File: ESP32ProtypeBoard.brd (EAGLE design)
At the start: 78.7 x 54.6 mm, 90 parts, among them IC1 ACT4088US-T, IC2 SI4431BDY, J4 VCC_TERMINAL, Q4 BSS138, U1 3.3V, U2 ESP-WROOM-32

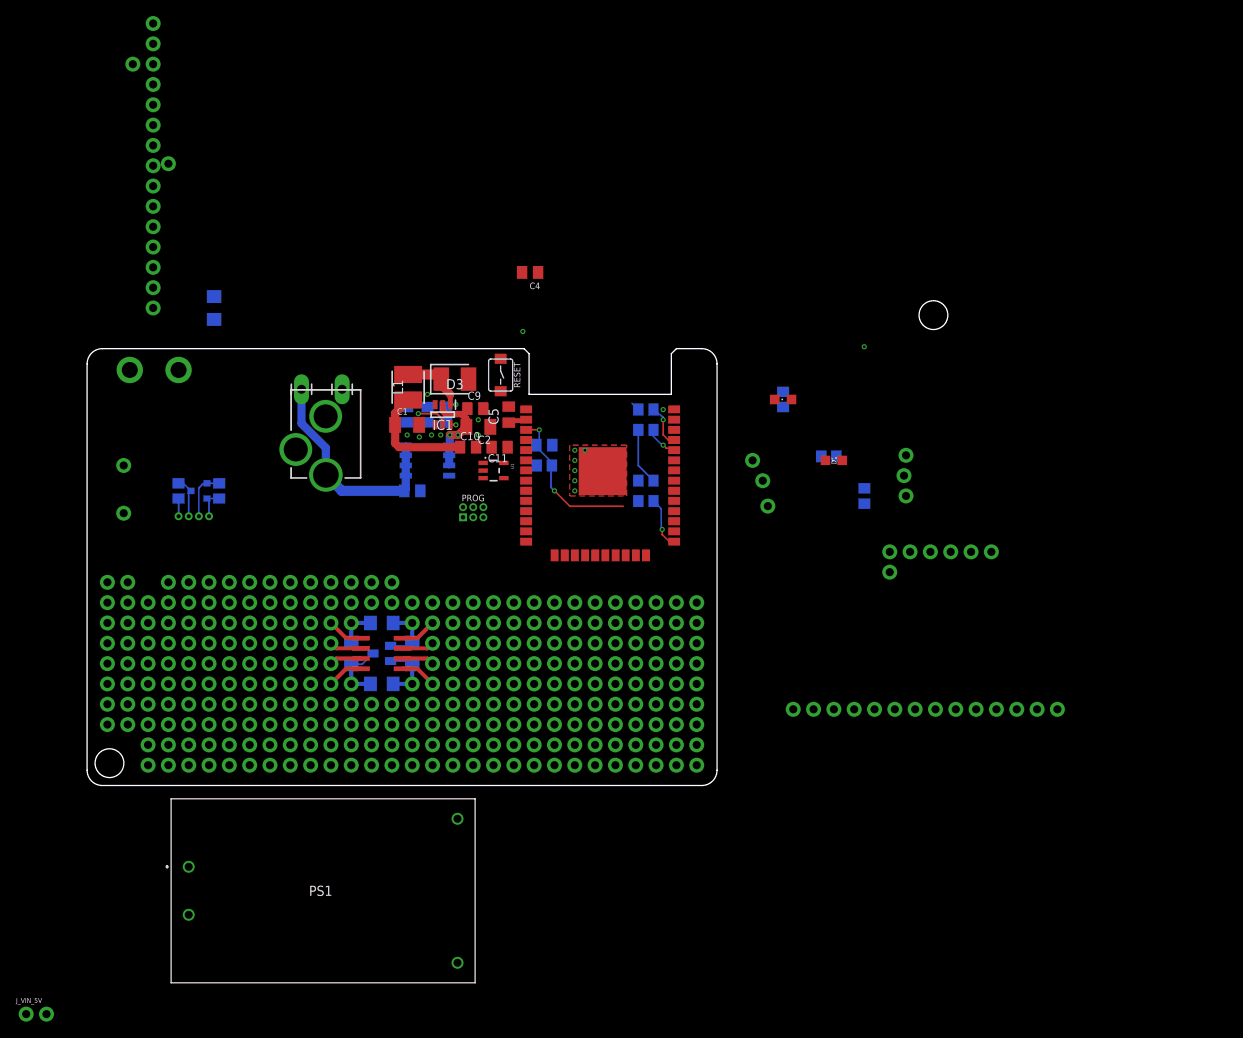
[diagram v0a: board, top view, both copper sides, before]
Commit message: A lot of wirings, no terminals in place yet
Power cascade looks good
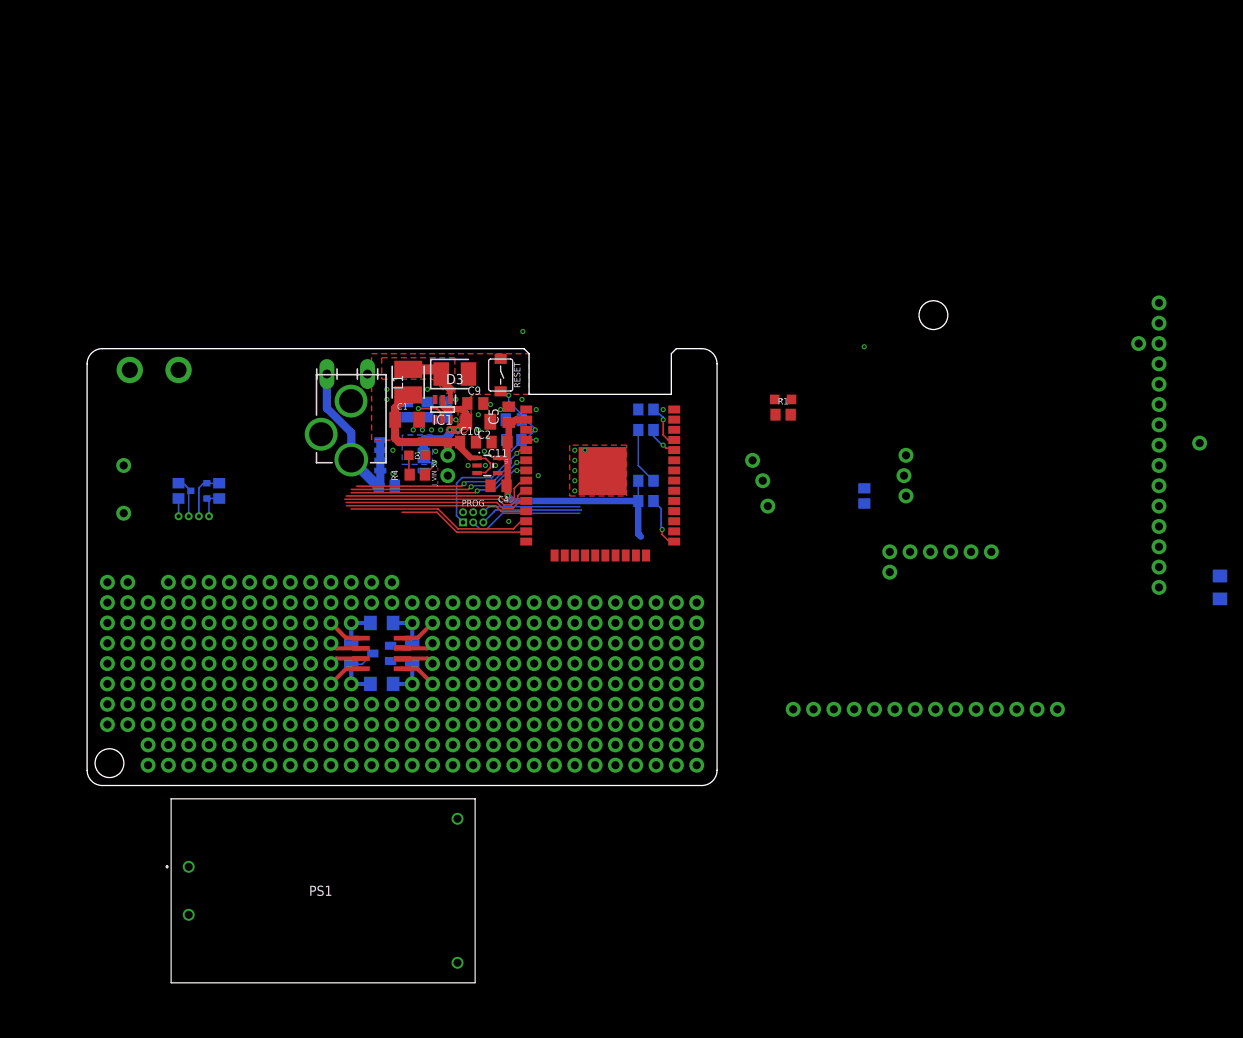
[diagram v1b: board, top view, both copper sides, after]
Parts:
- moved HI-LINK_GND 133.6 mm to (130.2, 42.8)
- moved +12V1 130.5 mm to (125.1, 57.8)
- moved J11 130.5 mm to (125.1, 24.8)
- moved J59 130.5 mm to (125.1, 55.2)
- moved R6 130.5 mm to (132.7, 24.8)
- moved J_VIN_5V 85.5 mm to (36.2, 38.7), turned to 90 degrees
- moved D1 52.1 mm to (32.4, 41.3), turned to 270 degrees
- moved R4 51.5 mm to (32.4, 38.9), flipped to the top, turned to 180 degrees
- moved C4 27.0 mm to (42.5, 37.5)
- moved C6 4.96 mm to (44.5, 45.7), turned to 180 degrees
- moved R5 4.96 mm to (44.5, 43.2)
- moved J10 3.70 mm to (24.1, 54.6)
- moved J3 3.70 mm to (26.2, 51.4)
- moved J4 3.70 mm to (21.1, 51.4)
- moved C8 3.24 mm to (28.6, 37.5)
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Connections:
- net N$50 renamed PWR_LED
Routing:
- net +3V3: track 2.34 -> 36.9 mm, vias 2 -> 3
- net IO32: track 0.00 -> 24.6 mm
- net IO33: track 0.00 -> 23.9 mm
- net IO39: track 0.00 -> 23.4 mm, vias 0 -> 2
- net IO34: track 0.00 -> 23.4 mm, vias 0 -> 2
- net IO27: track 0.00 -> 23.3 mm
- net IO25: track 0.00 -> 23.2 mm
- net IO35: track 0.00 -> 23.0 mm, vias 0 -> 2
- net IO26: track 0.00 -> 22.8 mm
- net IO14: track 0.00 -> 16.6 mm
- net PROG_TXD: track 1.11 -> 14.5 mm
- net PROG_RXD: track 7.14 -> 20.0 mm
- net IO0: track 6.50 -> 18.9 mm
- net +5V: track 14.4 -> 23.8 mm
- net EN: track 19.9 -> 26.8 mm
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- added copper zone on layer 1, net +12V
- added copper zone on layer 16, net +12V
- added copper zone on layer 1, net SW
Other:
- board text added: "VIN"

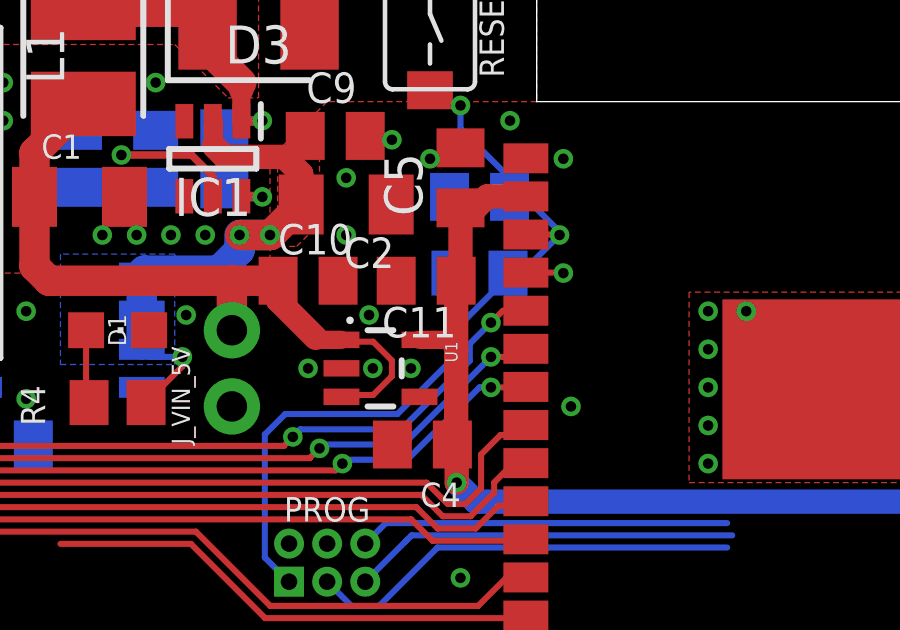
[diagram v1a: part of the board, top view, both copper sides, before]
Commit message: added missing 3v3 connection
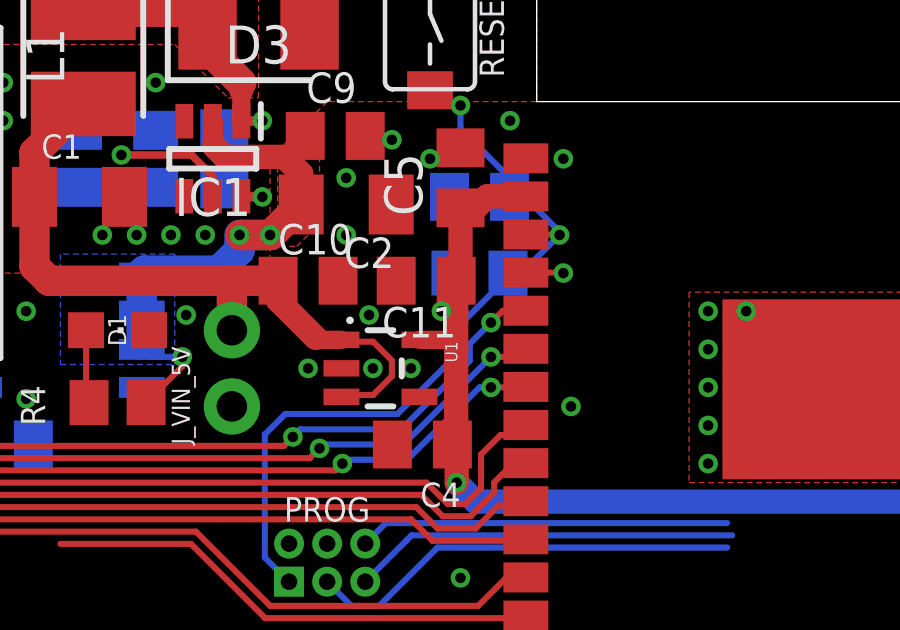
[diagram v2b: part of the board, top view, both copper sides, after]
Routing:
- net +3V3: track 36.9 -> 38.8 mm, vias 3 -> 4
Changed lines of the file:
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@@
 <wire x1="44.323" y1="35.56" x2="60.01" y2="35.56" width="0.8128" layer="16"/>
 <wire x1="43.672" y1="37.592" x2="43.545" y2="37.465" width="0.8128" layer="1"/>
-<wire x1="43.672" y1="42.926" x2="43.672" y2="40.64" width="0.8128" layer="1"/>
+<wire x1="43.672" y1="42.926" x2="43.672" y2="41.91" width="0.8128" layer="1"/>
+<wire x1="43.672" y1="41.91" x2="43.672" y2="40.64" width="0.8128" layer="1"/>
 <wire x1="43.672" y1="37.592" x2="43.672" y2="40.64" width="0.8128" layer="1"/>
 <wire x1="43.672" y1="40.64" x2="43.357" y2="40.955" width="0.6096" layer="1"/>
@@
 <wire x1="60.01" y1="31.43" x2="60.325" y2="31.115" width="0.8128" layer="16"/>
 <wire x1="60.01" y1="35.56" x2="60.01" y2="38.1" width="0.2032" layer="16"/>
+<wire x1="43.5" y1="43.18" x2="43.5" y2="42.23" width="0.2032" layer="16"/>
+<wire x1="43.5" y1="42.23" x2="43.18" y2="41.91" width="0.2032" layer="16"/>
+<via x="43.18" y="41.91" extent="1-16" drill="0.35"/>
+<wire x1="43.18" y1="41.91" x2="43.672" y2="41.91" width="0.2032" layer="1"/>
 <wire x1="125.095" y1="29.845" x2="125.095" y2="55.245" width="0" layer="19" extent="1-1"/>
 <wire x1="109.855" y1="9.525" x2="125.095" y2="29.845" width="0" layer="19" extent="1-1"/>
@@
 <wire x1="88.249" y1="54.845" x2="79.055" y2="46.355" width="0" layer="19" extent="1-1"/>
 <wire x1="60.01" y1="38.1" x2="79.055" y2="46.355" width="0" layer="19" extent="1-16"/>
-<wire x1="43.5" y1="43.18" x2="43.672" y2="42.926" width="0" layer="19" extent="1-16"/>
 <wire x1="45.577" y1="56.75" x2="45.995" y2="45.735" width="0" layer="19" extent="1-1"/>
 </signal>

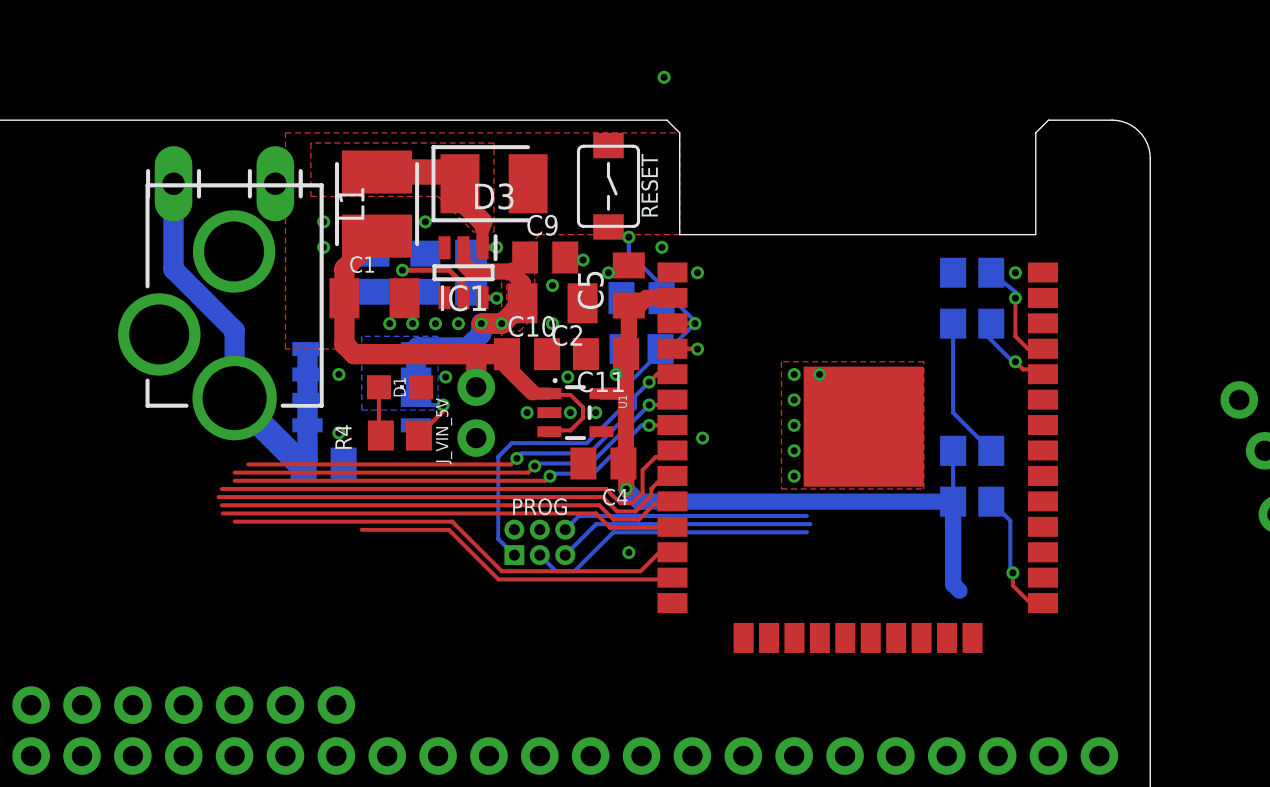
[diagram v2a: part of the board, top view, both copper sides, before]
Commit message: added missing FB connection
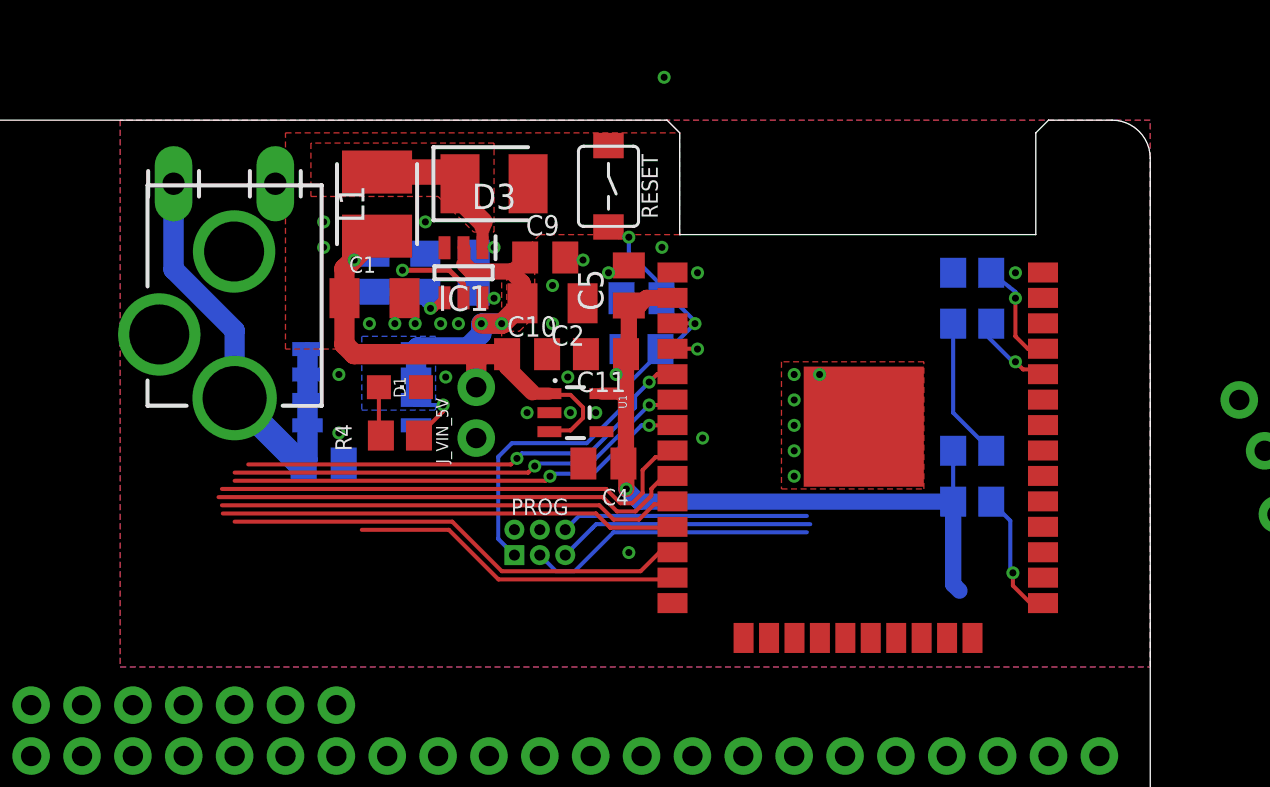
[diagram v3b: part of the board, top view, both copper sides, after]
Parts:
- moved C7 0.13 mm to (36.1, 47.0)
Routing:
- net FB: track 0.00 -> 4.39 mm, vias 0 -> 1
- net +5V: track 23.8 -> 25.0 mm, vias 0 -> 1
- net GND: vias 30 -> 31
- added copper zone on layer 16, net GND

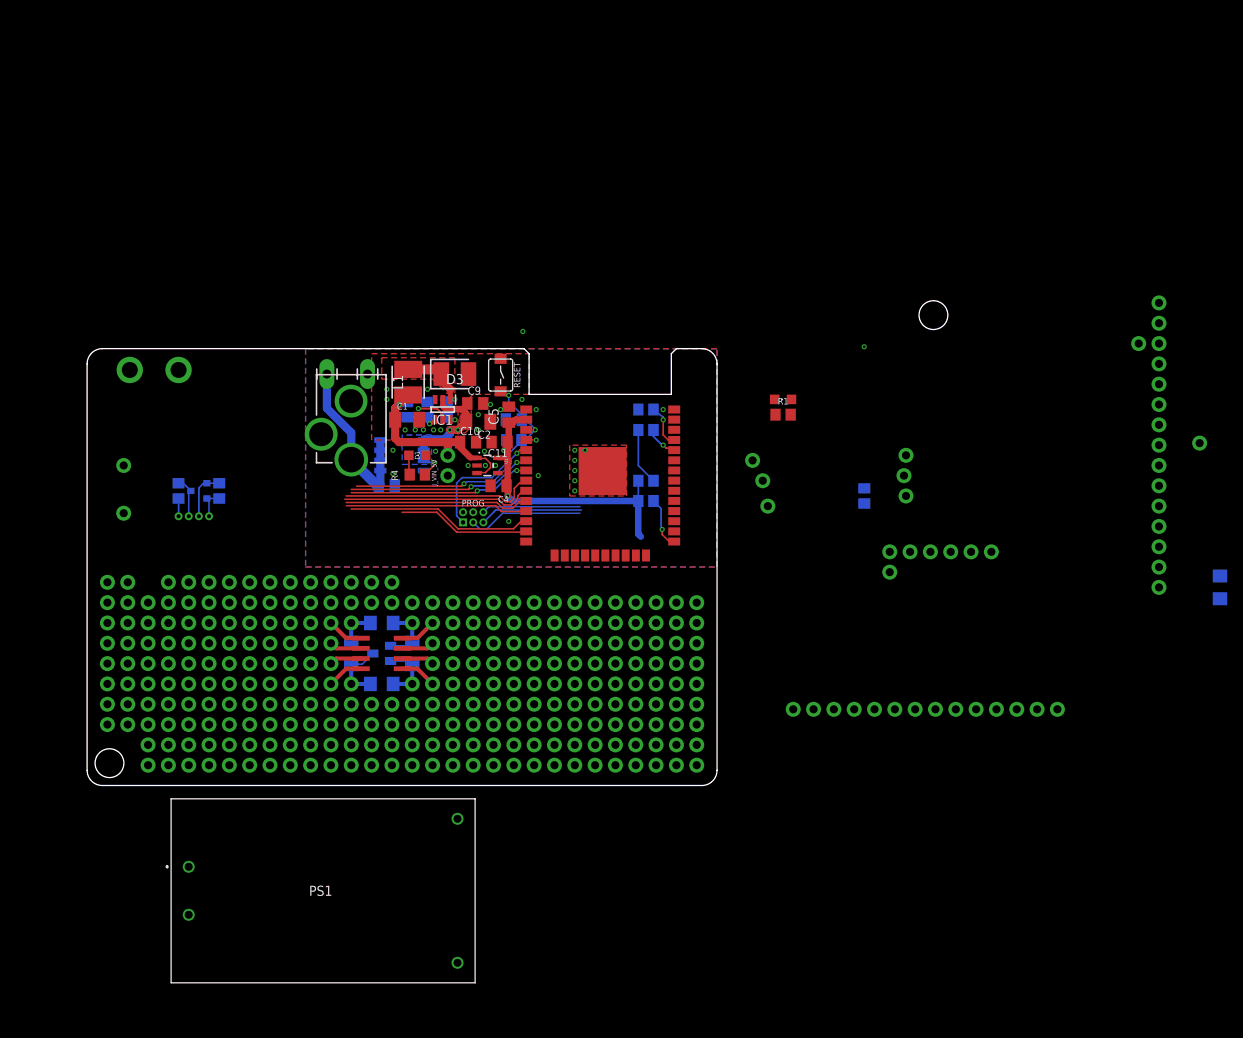
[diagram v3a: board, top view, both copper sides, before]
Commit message: Fixed terminal position, improved gnd traces
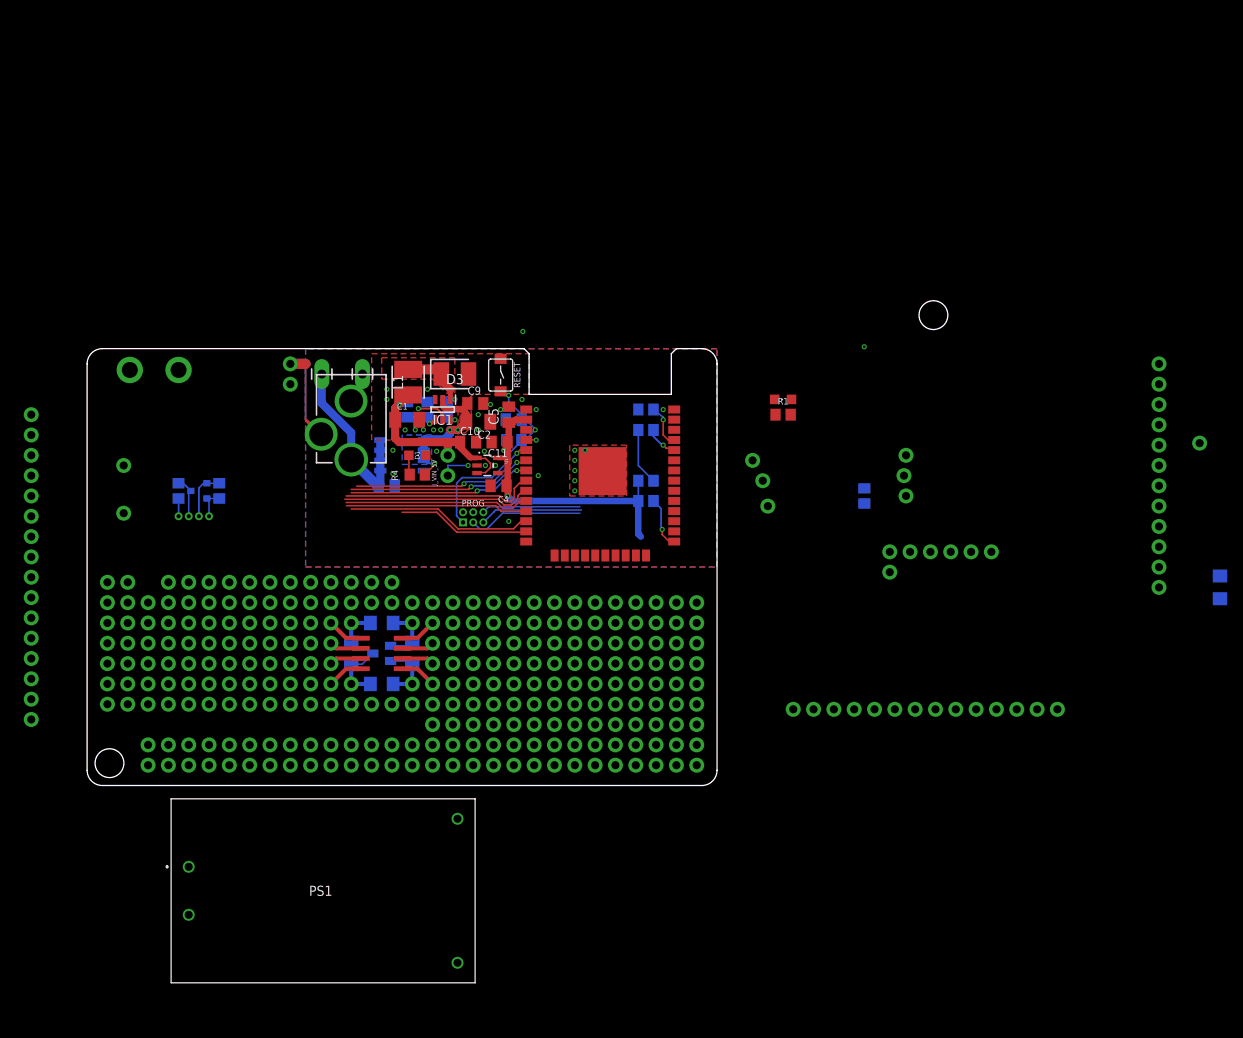
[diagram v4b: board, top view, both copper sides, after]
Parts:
- removed +12V1, J59: (no value), SparkFun-Connectors:1X02_NO_SILK
- added J_12V1: (no value), SparkFun-Connectors:1X02_NO_SILK
- moved J14 9.55 mm to (-15.9, 8.26), turned to 90 degrees
- moved J4 0.64 mm to (20.4, 51.4)
- moved J3 0.63 mm to (25.5, 51.4)
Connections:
- net +12V: now also J_12V1.2; no longer +12V1.2
- net +3V3: no longer J59.1
- net GND: now also J_12V1.1; no longer +12V1.1
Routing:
- net GND: track 4.01 -> 31.0 mm
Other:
- board text removed: "VCC-IN"
